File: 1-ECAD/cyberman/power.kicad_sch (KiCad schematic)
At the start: 8 parts, among them U2 BQ25896RTWR

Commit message: power
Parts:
- added C19, C29, C33: 10uF, symbol Device:C
- added C20, C28, C32: 4.7uF, symbol Device:C
- added C21: 470n, symbol Device:C
- added C22, C26, C27, C30, C31: 2.2uF, symbol Device:C
- added C23, C24, C25: 1uF, symbol Device:C
- added L4, L5: 470nH, symbol Device:L
- added NT1, NT2: NetTie_2, symbol Device:NetTie_2
- added R10, R11: 100k, symbol Device:R
- added R12, R14, R5, R6, R8, R9: 10k, symbol Device:R
- added R13: 100R, symbol Device:R
- added R3: 5.23k, symbol Device:R
- added R4: 30.1k, symbol Device:R
- added R7: 10m, symbol Device:R
- added TP1, TP2, TP3, TP4: TestPoint, symbol Connector:TestPoint
- added U10: DMN313DLT-7, symbol 0_CI_smd:DMN313DLT-7
- added U3: S3B-ZR-SM4A-TF, symbol 0_connector_smd:S3B-ZR-SM4A-TF
- added U4: BQ27220YZFR, symbol 0_CI_smd:BQ27220YZFR
- added U5: RS3221-3.3YF3, symbol 0_converterDCDC:RS3221-3.3YF3
- added U6, U7: LM3281YFQR, symbol 0_converterDCDC:LM3281YFQR
- added U8: MMDT2907A-7-F, symbol 0_CI_smd:MMDT2907A-7-F
- added U9: DMP1045U-7, symbol 0_CI_smd:DMP1045U-7
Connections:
- net GND: now also R2.1, U2. (PAD), U2.17 (PGND), U2.18 (PGND), U2.9 (~{CE}), C19.2, C20.2, C21.2, C22.2, C23.2, C24.2, C25.2, C28.2, C29.2, C32.2, C33.2, NT1.2, NT2.2, R10.1, R11.2, R14.2, R4.2, R6.2, U10.S, U3.3 (GND), U4.B2 (VSS), U5.1 (GND); no longer R2.2
- net VDC: now also C26.1, C30.1, R12.1, U6.A2 (VIN), U6.B1 (MODE), U7.A2 (VIN), U7.B1 (MODE), U7.C1 (EN)
- net VBUS: now reaches C14.1, C15.1, U2.1 (VBUS)
- net VBUS: now also U8.1, U9.S
- net at U2.10 (ILIM): now also R2.2; no longer R2.1
- net at U2.11 (TS): now also R3.1, R4.1, U3.2 (Temperature)
- net BUTTON_BACK: now reaches U2.12 (~{QON})
- net at U2.13 (BAT): now also U2.14 (BAT), C19.1, C24.1, R7.1, U4.C2 (SRN), U5.IN (3)
- net at U2.22 (REGN): now also C20.1, R3.2
- net at U2.3 (~{PG}): now also TP2.1
- net at U2.4 (STAT): now also TP1.1
- net SCL1: now reaches U2.5 (SCL)
- net SCL1: now also U4.A3 (SCL)
- net SDA1: now reaches U2.6 (SDA)
- net SDA1: now also U4.A2 (SDA)
- net at U2.7 (INT): now also R9.2, TP3.1
- net at U2.8 (OTG): now also R12.2, TP4.1, U10.D
- new net: R10.2, U8.6, U9.G
- new net: R13.2, R14.1, U10.G
- new net: C21.1, C22.1, U4.B3 (VDD)
- new net: L5.1, U7.B2 (SW)
- new net: R5.2, U4.A1 (GPOUT)
- new net: R6.1, U4.B1 (BIN)
- new net: L4.1, U6.B2 (SW)
- new net: R11.1, U8.2, U8.3, U8.5
- new net +3V3: C31.1, C32.1, C33.1, L5.2, R5.1, R8.1, R9.1, U7.A1 (FB)
- new net +BATT: C23.1, R7.2, U3.1 (BAT), U4.C1 (SRP), U4.C3 (BAT)
- new net EXT_3V3: C27.1, C28.1, C29.1, L4.2, U6.A1 (FB)
- new net GNDPWR: C30.2, NT2.1
- new net GNDPWR_EXT: C26.2, C27.2, C31.2, NT1.1, U6.C2 (GND), U7.C2 (GND)
- new net LDO_3V3: C25.1, U5.2 (OUT)
- new net PERIPH_PWR: R8.2, U6.C1 (EN)
- new net VUSB_5V: R13.1, U8.4, U9.D
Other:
- moved on the sheet: C14, C15, C16, C17, C18, L3, R2, U2

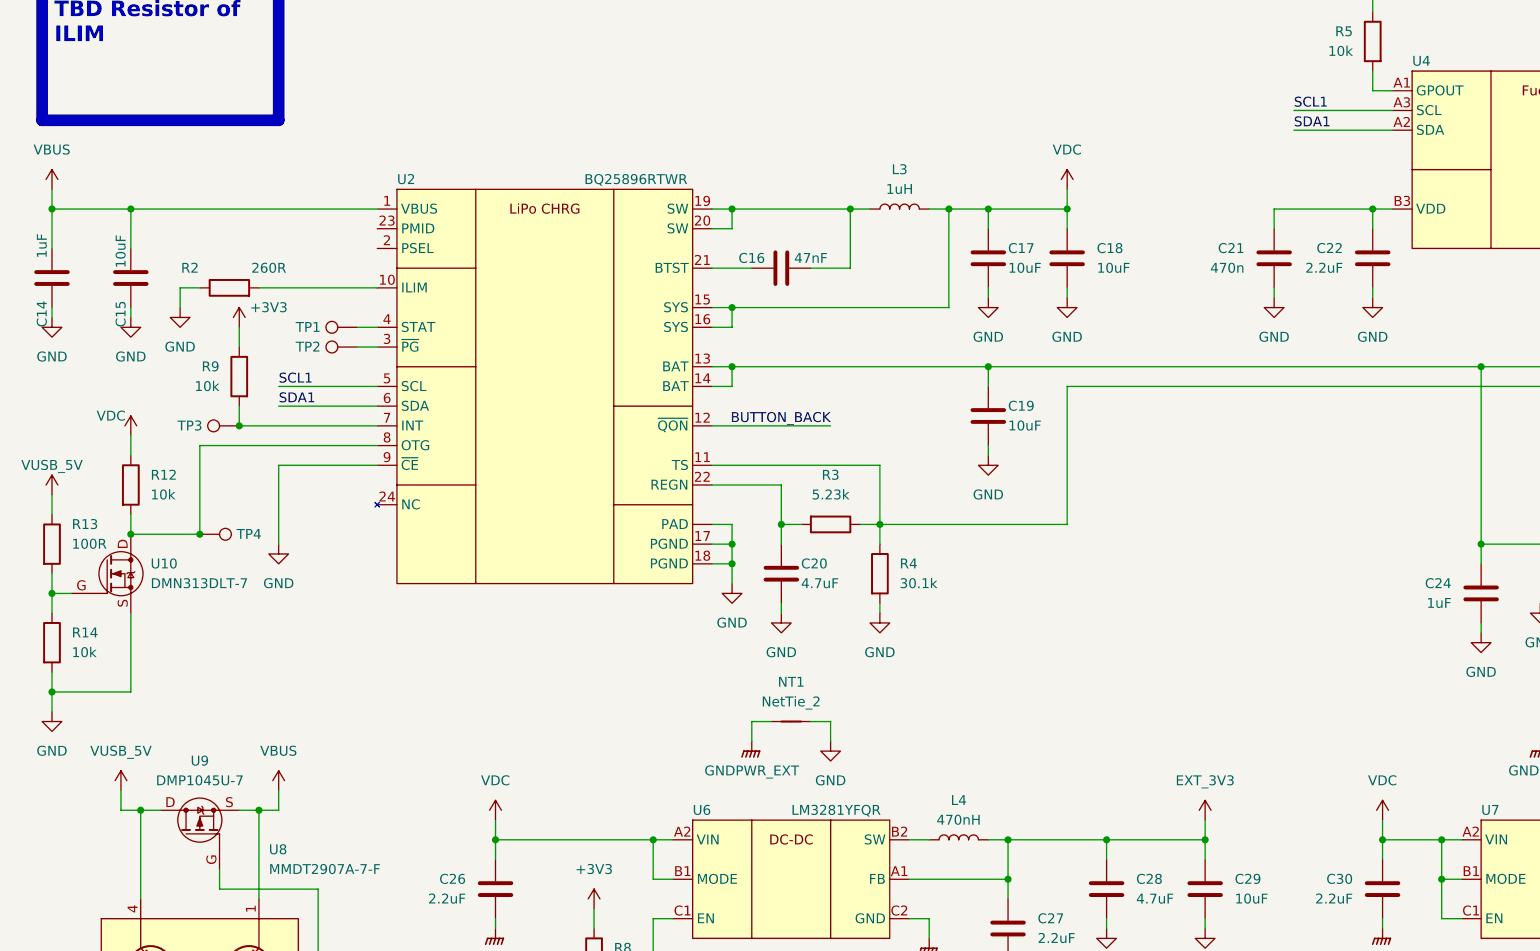
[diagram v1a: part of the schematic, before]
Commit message: microSD and LCD connector
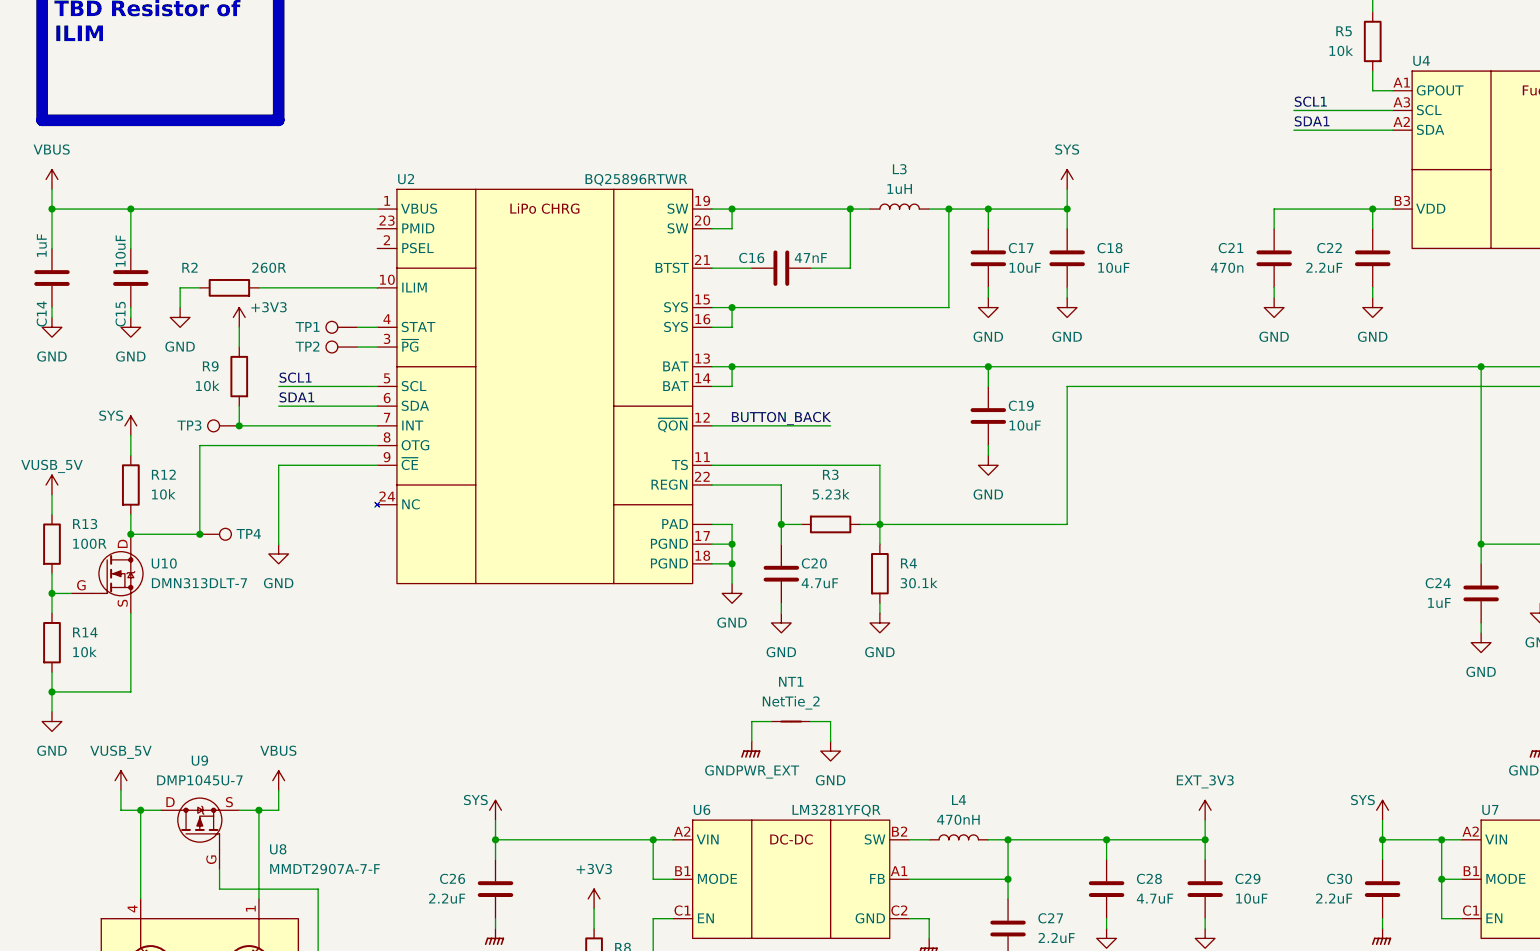
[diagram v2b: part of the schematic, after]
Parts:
- U3: kode PN DOTCONN001 -> DOTCON001
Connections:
- net VDC renamed SYS
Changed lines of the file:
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@@
 	)
 	(symbol
+		(lib_id "power:VDC")
+		(at 76.2 127 0)
+		(unit 1)
+		(exclude_from_sim no)
+		(in_bom yes)
+		(on_board yes)
+		(dnp no)
+		(property "Reference" "#PWR046"
+			(at 76.2 130.81 0)
+			(effects
+				(font
+					(size 1.27 1.27)
+				)
+				(hide yes)
+			)
+		)
+		(property "Value" "SYS"
+			(at 73.66 124.46 0)
+			(effects
+				(font
+					(size 1.27 1.27)
+				)
+			)
+		)
+		(property "Footprint" ""
+			(at 76.2 127 0)
+			(effects
+				(font
+					(size 1.27 1.27)
+				)
+				(hide yes)
+			)
+		)
+		(property "Datasheet" ""
+			(at 76.2 127 0)
+			(effects
+				(font
+					(size 1.27 1.27)
+				)
+				(hide yes)
+			)
+		)
+		(property "Description" "Power symbol creates a global label with name \"VDC\""
+			(at 76.2 127 0)
+			(effects
+				(font
+					(size 1.27 1.27)
+				)
+				(hide yes)
+			)
+		)
+		(pin "1"
+		)
+		(instances
+			(project "cyberman"
+				(path "/0650c7a8-acba-429c-9f8e-eec0baf0bc1c/fede4c36-00cc-4d3d-b71c-5243ba232202/257dfcdf-7056-4a45-9902-57dc3726f775"
+					(reference "#PWR046")
+					(unit 1)
+				)
+			)
+		)
+	)
+	(symbol
 		(lib_id "power:+3V3")
 		(at 246.38 88.9 0)
@@
 			)
 		)
-		(property "Value" "VDC"
+		(property "Value" "SYS"
 			(at 26.67 74.93 0)
 			(effects
@@
 	)
 	(symbol
+		(lib_id "power:VDC")
+		(at 190.5 127 0)
+		(unit 1)
+		(exclude_from_sim no)
+		(in_bom yes)
+		(on_board yes)
+		(dnp no)
+		(property "Reference" "#PWR056"
+			(at 190.5 130.81 0)
+			(effects
+				(font
+					(size 1.27 1.27)
+				)
+				(hide yes)
+			)
+		)
+		(property "Value" "SYS"
+			(at 187.96 124.46 0)
+			(effects
+				(font
+					(size 1.27 1.27)
+				)
+			)
+		)
+		(property "Footprint" ""
+			(at 190.5 127 0)
+			(effects
+				(font
+					(size 1.27 1.27)
+				)
+				(hide yes)
+			)
+		)
+		(property "Datasheet" ""
+			(at 190.5 127 0)
+			(effects
+				(font
+					(size 1.27 1.27)
+				)
+				(hide yes)
+			)
+		)
+		(property "Description" "Power symbol creates a global label with name \"VDC\""
+			(at 190.5 127 0)
+			(effects
+				(font
+					(size 1.27 1.27)
+				)
+				(hide yes)
+			)
+		)
+		(pin "1"
+		)
+		(instances
+			(project "cyberman"
+				(path "/0650c7a8-acba-429c-9f8e-eec0baf0bc1c/fede4c36-00cc-4d3d-b71c-5243ba232202/257dfcdf-7056-4a45-9902-57dc3726f775"
+					(reference "#PWR056")
+					(unit 1)
+				)
+			)
+		)
+	)
+	(symbol
 		(lib_id "Device:R")
 		(at 125.73 95.25 0)
@@
 	)
 	(symbol
-		(lib_id "power:VDC")
-		(at 76.2 127 0)
-		(unit 1)
-		(exclude_from_sim no)
-		(in_bom yes)
-		(on_board yes)
-		(dnp no)
-		(fields_autoplaced yes)
-		(property "Reference" "#PWR046"
-			(at 76.2 130.81 0)
-			(effects
-				(font
-					(size 1.27 1.27)
-				)
-				(hide yes)
-			)
-		)
-		(property "Value" "VDC"
-			(at 76.2 121.92 0)
-			(effects
-				(font
-					(size 1.27 1.27)
-				)
-			)
-		)
-		(property "Footprint" ""
-			(at 76.2 127 0)
-			(effects
-				(font
-					(size 1.27 1.27)
-				)
-				(hide yes)
-			)
-		)
-		(property "Datasheet" ""
-			(at 76.2 127 0)
-			(effects
-				(font
-					(size 1.27 1.27)
-				)
-				(hide yes)
-			)
-		)
-		(property "Description" "Power symbol creates a global label with name \"VDC\""
-			(at 76.2 127 0)
-			(effects
-				(font
-					(size 1.27 1.27)
-				)
-				(hide yes)
-			)
-		)
-		(pin "1"
-		)
-		(instances
-			(project ""
-				(path "/0650c7a8-acba-429c-9f8e-eec0baf0bc1c/fede4c36-00cc-4d3d-b71c-5243ba232202/257dfcdf-7056-4a45-9902-57dc3726f775"
-					(reference "#PWR046")
-					(unit 1)
-				)
-			)
-		)
-	)
-	(symbol
 		(lib_id "power:GND")
 		(at 19.05 113.03 0)
@@
 			)
 		)
-		(property "kode PN" "DOTCONN001"
+		(property "kode PN" "DOTCON001"
 			(at 266.7 66.04 0)
 			(effects
@@
 	(symbol
 		(lib_id "power:VDC")
-		(at 190.5 127 0)
-		(unit 1)
-		(exclude_from_sim no)
-		(in_bom yes)
-		(on_board yes)
-		(dnp no)
-		(fields_autoplaced yes)
-		(property "Reference" "#PWR056"
-			(at 190.5 130.81 0)
-			(effects
-				(font
-					(size 1.27 1.27)
-				)
-				(hide yes)
-			)
-		)
-		(property "Value" "VDC"
-			(at 190.5 121.92 0)
-			(effects
-				(font
-					(size 1.27 1.27)
-				)
-			)
-		)
-		(property "Footprint" ""
-			(at 190.5 127 0)
-			(effects
-				(font
-					(size 1.27 1.27)
-				)
-				(hide yes)
-			)
-		)
-		(property "Datasheet" ""
-			(at 190.5 127 0)
-			(effects
-				(font
-					(size 1.27 1.27)
-				)
-				(hide yes)
-			)
-		)
-		(property "Description" "Power symbol creates a global label with name \"VDC\""
-			(at 190.5 127 0)
-			(effects
-				(font
-					(size 1.27 1.27)
-				)
-				(hide yes)
-			)
-		)
-		(pin "1"
-		)
-		(instances
-			(project "cyberman"
-				(path "/0650c7a8-acba-429c-9f8e-eec0baf0bc1c/fede4c36-00cc-4d3d-b71c-5243ba232202/257dfcdf-7056-4a45-9902-57dc3726f775"
-					(reference "#PWR056")
-					(unit 1)
-				)
-			)
-		)
-	)
-	(symbol
-		(lib_id "power:VDC")
 		(at 149.86 45.72 0)
 		(unit 1)
@@
 			)
 		)
-		(property "Value" "VDC"
+		(property "Value" "SYS"
 			(at 149.86 40.64 0)
 			(effects

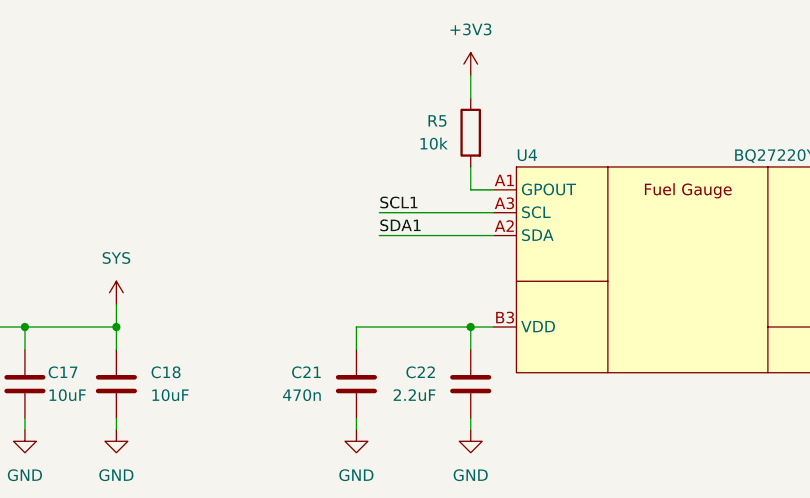
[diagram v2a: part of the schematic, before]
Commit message: add sensor page
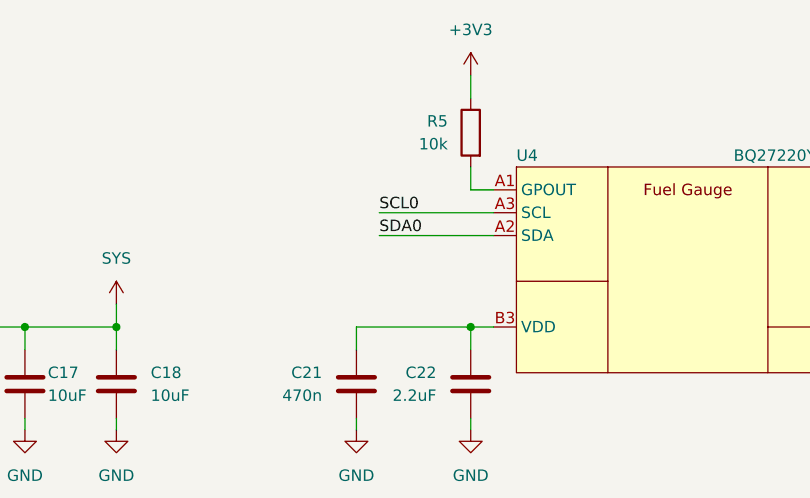
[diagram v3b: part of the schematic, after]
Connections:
- net SCL1: no longer U4.A3 (SCL)
- net SDA1: no longer U4.A2 (SDA)
- new net SCL0: U4.A3 (SCL)
- new net SDA0: U4.A2 (SDA)
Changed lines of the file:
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@@
 		)
 	)
-	(label "SDA1"
+	(label "SDA0"
 		(at 179.07 38.1 0)
 		(fields_autoplaced yes)
@@
 		)
 	)
-	(label "SCL1"
+	(label "SCL0"
 		(at 179.07 35.56 0)
 		(fields_autoplaced yes)

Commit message: hey
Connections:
- net SCL0 renamed I2C_BOARD.SCL
- net SCL1 renamed I2C_AUX.SCL
- net SDA0 renamed I2C_BOARD.SDA
- net SDA1 renamed I2C_AUX.SDA
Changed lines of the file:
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@@
 		(color 0 0 0 0)
 	)
+	(bus_entry
+		(at 76.2 181.61)
+		(size -2.54 2.54)
+		(stroke
+			(width 0)
+			(type default)
+		)
+	)
+	(bus_entry
+		(at 31.75 189.23)
+		(size -2.54 2.54)
+		(stroke
+			(width 0)
+			(type default)
+		)
+	)
+	(bus_entry
+		(at 31.75 186.69)
+		(size -2.54 2.54)
+		(stroke
+			(width 0)
+			(type default)
+		)
+	)
+	(bus_entry
+		(at 76.2 171.45)
+		(size -2.54 2.54)
+		(stroke
+			(width 0)
+			(type default)
+		)
+	)
+	(bus_entry
+		(at 76.2 184.15)
+		(size -2.54 2.54)
+		(stroke
+			(width 0)
+			(type default)
+		)
+	)
+	(bus_entry
+		(at 76.2 168.91)
+		(size -2.54 2.54)
+		(stroke
+			(width 0)
+			(type default)
+		)
+	)
 	(wire
 		(pts
@@
 	(wire
 		(pts
+			(xy 17.78 189.23) (xy 29.21 189.23)
+		)
+		(stroke
+			(width 0)
+			(type default)
+		)
+	)
+	(wire
+		(pts
 			(xy 234.95 33.02) (xy 256.54 33.02)
 		)
@@
 	(wire
 		(pts
+			(xy 58.42 173.99) (xy 73.66 173.99)
+		)
+		(stroke
+			(width 0)
+			(type default)
+		)
+	)
+	(wire
+		(pts
 			(xy 104.14 83.82) (xy 113.03 83.82)
 		)
@@
 	(wire
 		(pts
-			(xy 25.4 182.88) (xy 40.64 182.88)
-		)
-		(stroke
-			(width 0)
-			(type default)
-		)
-	)
-	(wire
-		(pts
 			(xy 132.08 48.26) (xy 134.62 48.26)
 		)
@@
 		)
 	)
+	(bus
+		(pts
+			(xy 31.75 184.15) (xy 31.75 186.69)
+		)
+		(stroke
+			(width 0)
+			(type default)
+		)
+	)
+	(bus
+		(pts
+			(xy 76.2 179.07) (xy 76.2 181.61)
+		)
+		(stroke
+			(width 0)
+			(type default)
+		)
+	)
 	(wire
 		(pts
@@
 	(wire
 		(pts
-			(xy 25.4 185.42) (xy 40.64 185.42)
-		)
-		(stroke
-			(width 0)
-			(type default)
-		)
-	)
-	(wire
-		(pts
 			(xy 203.2 68.58) (xy 203.2 91.44)
 		)
@@
 		)
 	)
+	(bus
+		(pts
+			(xy 31.75 186.69) (xy 31.75 189.23)
+		)
+		(stroke
+			(width 0)
+			(type default)
+		)
+	)
 	(wire
 		(pts
@@
 	(wire
 		(pts
+			(xy 58.42 186.69) (xy 73.66 186.69)
+		)
+		(stroke
+			(width 0)
+			(type default)
+		)
+	)
+	(wire
+		(pts
 			(xy 21.59 97.79) (xy 19.05 97.79)
 		)
@@
 	(wire
 		(pts
-			(xy 179.07 38.1) (xy 191.77 38.1)
+			(xy 176.53 38.1) (xy 191.77 38.1)
 		)
 		(stroke
@@
 		)
 	)
+	(bus
+		(pts
+			(xy 76.2 181.61) (xy 76.2 184.15)
+		)
+		(stroke
+			(width 0)
+			(type default)
+		)
+	)
 	(wire
 		(pts
@@
 	(wire
 		(pts
-			(xy 179.07 35.56) (xy 191.77 35.56)
+			(xy 58.42 171.45) (xy 73.66 171.45)
+		)
+		(stroke
+			(width 0)
+			(type default)
+		)
+	)
+	(wire
+		(pts
+			(xy 176.53 35.56) (xy 191.77 35.56)
+		)
+		(stroke
+			(width 0)
+			(type default)
+		)
+	)
+	(wire
+		(pts
+			(xy 58.42 184.15) (xy 73.66 184.15)
 		)
 		(stroke
@@
 		)
 	)
+	(bus
+		(pts
+			(xy 76.2 168.91) (xy 76.2 171.45)
+		)
+		(stroke
+			(width 0)
+			(type default)
+		)
+	)
 	(wire
 		(pts
@@
 	(wire
 		(pts
+			(xy 17.78 191.77) (xy 29.21 191.77)
+		)
+		(stroke
+			(width 0)
+			(type default)
+		)
+	)
+	(wire
+		(pts
 			(xy 167.64 129.54) (xy 167.64 132.08)
 		)
@@
 	(wire
 		(pts
-			(xy 25.4 190.5) (xy 40.64 190.5)
-		)
-		(stroke
-			(width 0)
-			(type default)
-		)
-	)
-	(wire
-		(pts
 			(xy 220.98 114.3) (xy 220.98 116.84)
 		)
@@
 		)
 	)
+	(bus
+		(pts
+			(xy 76.2 166.37) (xy 76.2 168.91)
+		)
+		(stroke
+			(width 0)
+			(type default)
+		)
+	)
 	(wire
 		(pts
@@
 		(pts
 			(xy 176.53 48.26) (xy 189.23 48.26)
-		)
-		(stroke
-			(width 0)
-			(type default)
-		)
-	)
-	(wire
-		(pts
-			(xy 25.4 187.96) (xy 40.64 187.96)
 		)
 		(stroke
@@
 		)
 	)
-	(label "SDA1"
-		(at 48.26 73.66 0)
-		(fields_autoplaced yes)
-		(effects
-			(font
-				(size 1.27 1.27)
-			)
-			(justify left bottom)
-		)
-	)
 	(label "PERIPH_PWR"
 		(at 74.93 151.13 0)
@@
 		)
 	)
-	(label "SDA0"
-		(at 179.07 38.1 0)
+	(label "I2C_AUX.SDA"
+		(at 48.26 73.66 0)
 		(fields_autoplaced yes)
 		(effects
@@
 		)
 	)
-	(label "SDA1"
-		(at 25.4 185.42 0)
+	(label "I2C_BOARD.SCL"
+		(at 176.53 35.56 0)
 		(fields_autoplaced yes)
 		(effects
@@
 		)
 	)
-	(label "BUTTON_BACK"
-		(at 25.4 190.5 0)
+	(label "PWR.PERIPH"
+		(at 17.78 189.23 0)
+		(fields_autoplaced yes)
+		(effects
+			(font
+				(size 1.27 1.27)
+			)
+			(justify left bottom)
+		)
+	)
+	(label "I2C_BOARD.SCL"
+		(at 58.42 171.45 0)
+		(fields_autoplaced yes)
+		(effects
+			(font
+				(size 1.27 1.27)
+			)
+			(justify left bottom)
+		)
+	)
+	(label "PWR.RST"
+		(at 17.78 191.77 0)
 		(fields_autoplaced yes)
 		(effects
@@
 		)
 	)
-	(label "PERIPH_PWR"
-		(at 25.4 187.96 0)
+	(label "I2C_BOARD.SDA"
+		(at 176.53 38.1 0)
 		(fields_autoplaced yes)
 		(effects
@@
 		)
 	)
-	(label "SCL1"
+	(label "I2C_AUX.SCL"
 		(at 48.26 71.12 0)
 		(fields_autoplaced yes)
@@
 		)
 	)
-	(label "SCL1"
-		(at 25.4 182.88 0)
+	(label "I2C_BOARD.SDA"
+		(at 58.42 173.99 0)
 		(fields_autoplaced yes)
 		(effects
@@
 		)
 	)
-	(label "SCL0"
-		(at 179.07 35.56 0)
+	(label "I2C_AUX.SDA"
+		(at 58.42 186.69 0)
 		(fields_autoplaced yes)
 		(effects
@@
 		)
 	)
-	(global_label "PERIPH_PWR"
+	(label "I2C_AUX.SCL"
+		(at 58.42 184.15 0)
+		(fields_autoplaced yes)
+		(effects
+			(font
+				(size 1.27 1.27)
+			)
+			(justify left bottom)
+		)
+	)
+	(hierarchical_label "I2C_AUX{SCL SDA}"
 		(shape input)
-		(at 40.64 187.96 0)
+		(at 76.2 179.07 0)
 		(fields_autoplaced yes)
 		(effects
@@
 			(justify left)
 		)
-		(property "Intersheetrefs" "${INTERSHEET_REFS}"
-			(at 55.4785 187.96 0)
-			(effects
-				(font
-					(size 1.27 1.27)
-				)
-				(justify left)
-				(hide yes)
-			)
-		)
-	)
-	(global_label "BUTTON_BACK"
+	)
+	(hierarchical_label "I2C_BOARD{SCL SDA}"
 		(shape input)
-		(at 40.64 190.5 0)
+		(at 76.2 166.37 0)
 		(fields_autoplaced yes)
 		(effects
@@
 			(justify left)
 		)
-		(property "Intersheetrefs" "${INTERSHEET_REFS}"
-			(at 56.6881 190.5 0)
-			(effects
-				(font
-					(size 1.27 1.27)
-				)
-				(justify left)
-				(hide yes)
-			)
-		)
-	)
-	(global_label "SCL1"
+	)
+	(hierarchical_label "PWR{PERIPH RST}"
 		(shape input)
-		(at 40.64 182.88 0)
+		(at 31.75 184.15 0)
 		(fields_autoplaced yes)
 		(effects
@@
 			(justify left)
 		)
-		(property "Intersheetrefs" "${INTERSHEET_REFS}"
-			(at 48.3423 182.88 0)
-			(effects
-				(font
-					(size 1.27 1.27)
-				)
-				(justify left)
-				(hide yes)
-			)
-		)
-	)
-	(global_label "SDA1"
-		(shape bidirectional)
-		(at 40.64 185.42 0)
-		(fields_autoplaced yes)
-		(effects
-			(font
-				(size 1.27 1.27)
-			)
-			(justify left)
-		)
-		(property "Intersheetrefs" "${INTERSHEET_REFS}"
-			(at 49.5141 185.42 0)
-			(effects
-				(font
-					(size 1.27 1.27)
-				)
-				(justify left)
-				(hide yes)
-			)
-		)
-	)
+	)

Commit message: footpritn day
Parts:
- U2: footprint (none) -> 0_CI_smd:BQ25896RTWR; Supplier 1 PN (none) -> C181475; Supplier PN 1 C181475 -> (none)
- U4: footprint (none) -> 0_CI_smd:BQ27220YZFR; Supplier 1 PN (none) -> C181475; Supplier PN 1 C181475 -> (none)
- U5: footprint (none) -> 0_converter_DCDC:RS3221-3.3YF3
- U6, U7: footprint (none) -> 0_converter_DCDC:LM3281YFQR
- U8: footprint (none) -> 0_CI_smd:MMDT2907A-7-F
